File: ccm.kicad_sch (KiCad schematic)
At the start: 92 parts, among them J1 Conn_01x02_Socket, J10 Conn_01x02_Socket, J11 Conn_01x02_Socket, J12 Conn_01x02_Socket, J13 Conn_01x02_Socket, J15 Conn_01x02_Socket, J16 Conn_01x02_Socket, J17 Conn_01x02_Socket, J18 Conn_01x02_Socket, J19 Conn_01x02_Socket, J2 Conn_01x02_Socket, J20 Conn_01x02_Socket, J21 Conn_01x02_Socket, J22 Conn_01x02_Socket, J23 Conn_01x02_Socket, J24 Conn_01x02_Socket, J3 Conn_01x02_Socket, J4 Conn_01x04_Socket, J5 Conn_01x02_Socket, J6 Conn_01x02_Socket, J7 Conn_01x02_Socket, J8 Conn_01x04_Socket, J9 Conn_01x02_Socket, Q1 IRLZ34N, Q2 IRLZ34N, Q3 IRLZ34N, Q4 MMBT3904, Q5 MMBT3904, U1 Teensy4.1, U2 PAM8302AAY, U3 SN65HVD230, U4 SN65HVD230, U5 LM1117DT-5.0

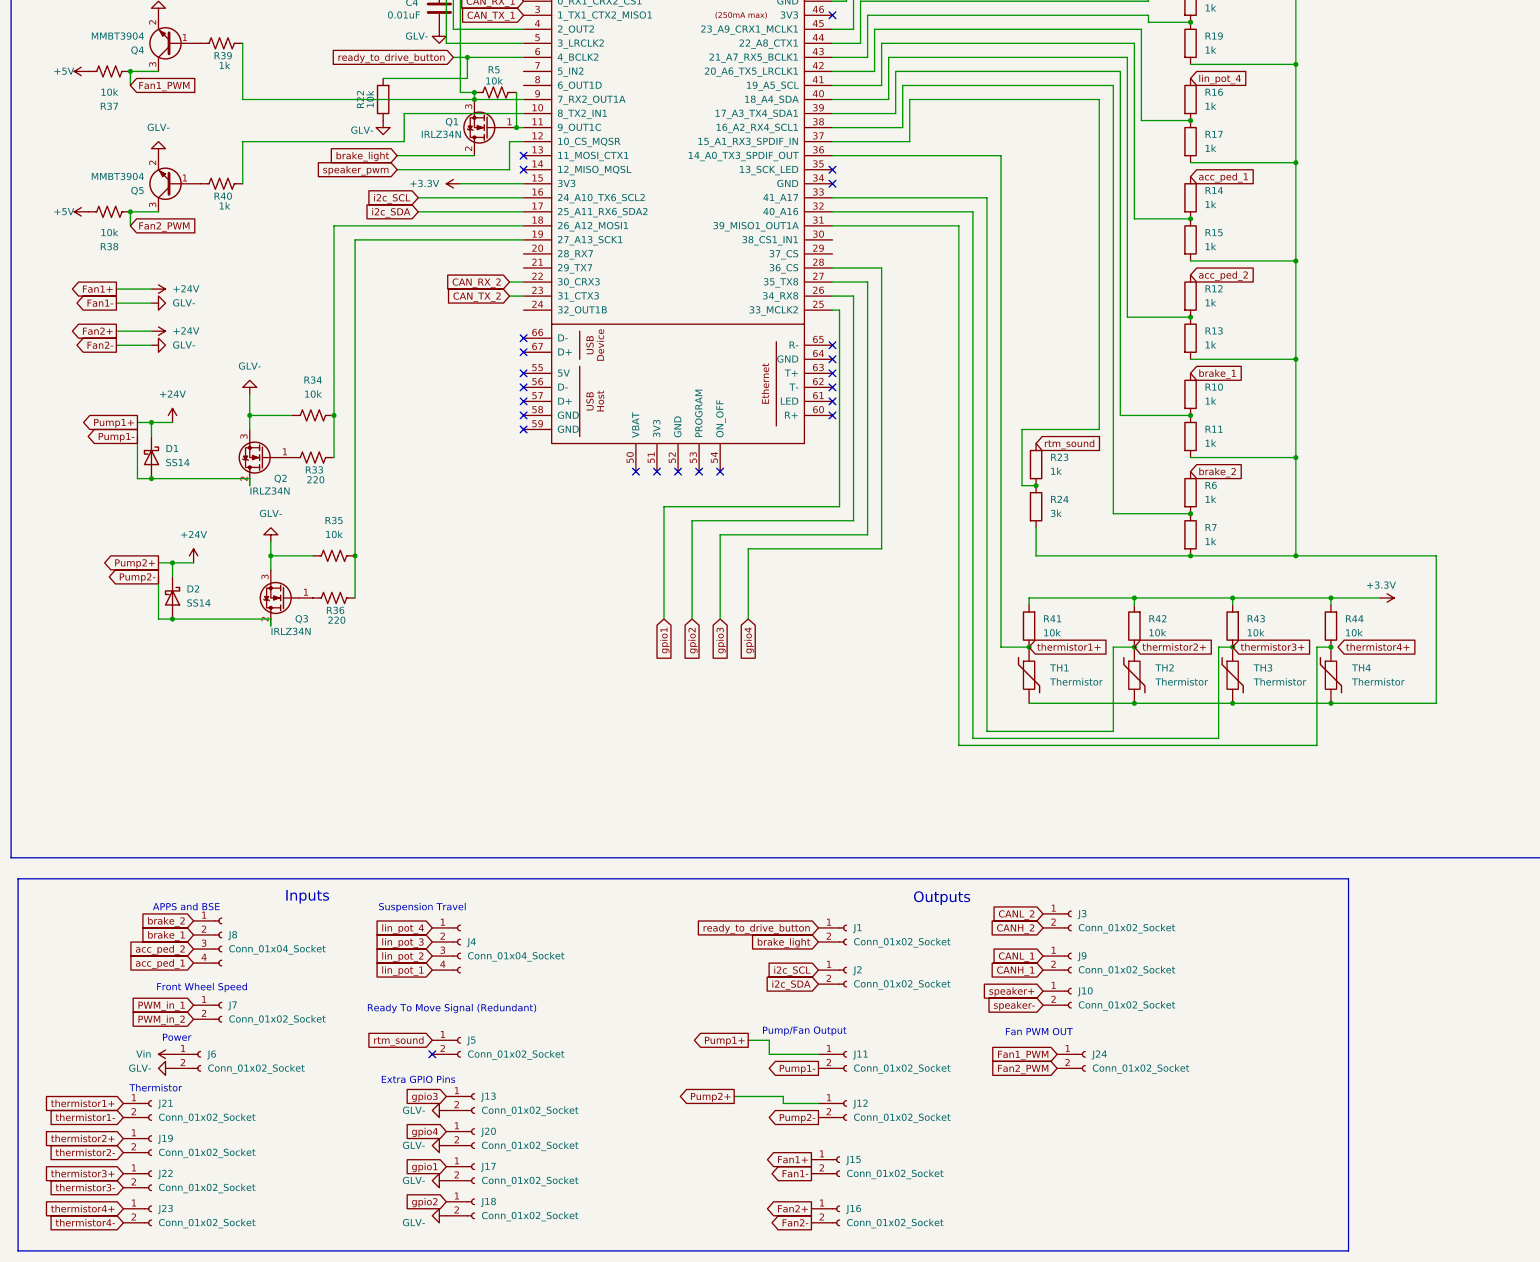
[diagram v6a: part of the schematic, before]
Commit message: leftside routing complete
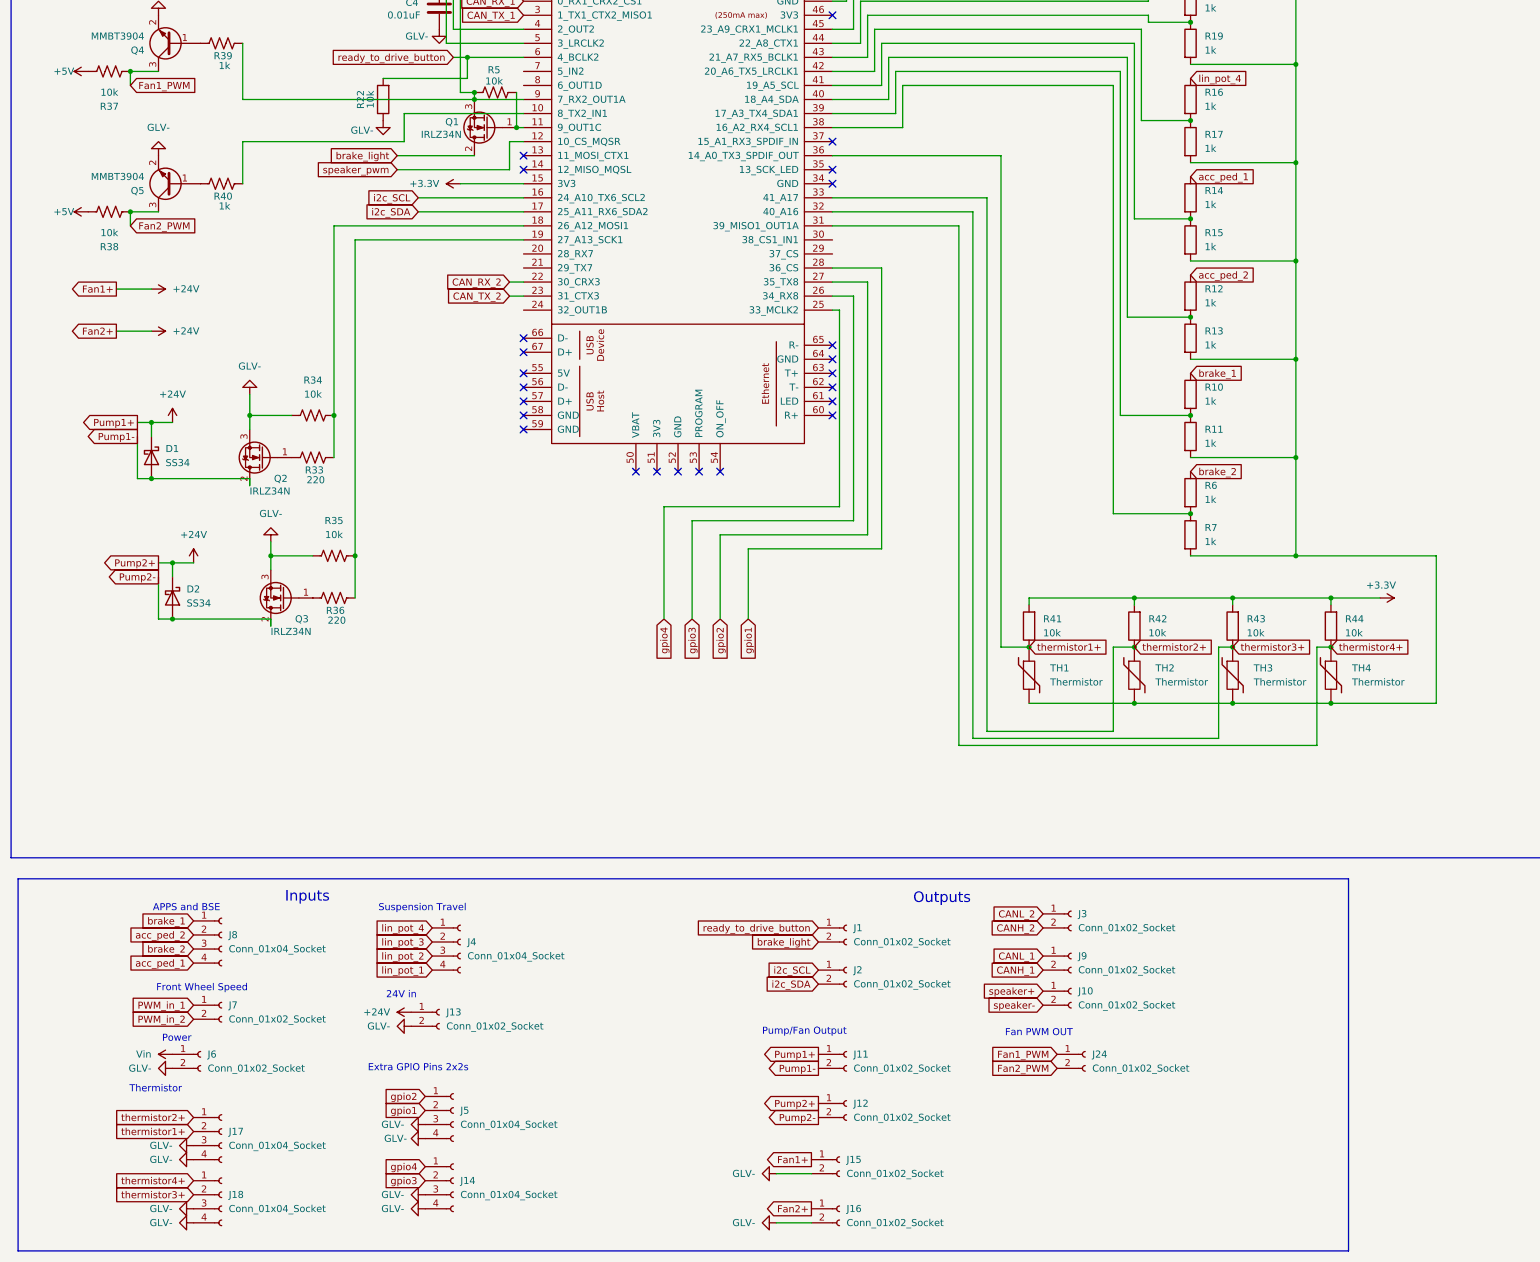
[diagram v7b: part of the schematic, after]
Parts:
- removed D1, D2: SS14, Diode_SMD:D_SMA, symbol Diode:SS14
- removed J17, J18, J19, J20, J21, J22, J23, J5: Conn_01x02_Socket, Connector_Molex:Molex_Mini-Fit_Jr_5566-02A2_2x01_P4.20mm_Vertical, symbol Connector:Conn_01x02_Socket
- removed R23: 1k, Resistor_SMD:R_0805_2012Metric, symbol Device:R
- removed R24: 3k, Resistor_SMD:R_0805_2012Metric, symbol Device:R
- added D1, D2: SS34, Diode_SMD:D_SMA, symbol Diode:SS34
- added J14, J17, J18, J5: Conn_01x04_Socket, Connector_Molex:Molex_Mini-Fit_Jr_5566-04A2_2x02_P4.20mm_Vertical, symbol Connector:Conn_01x04_Socket
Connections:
- net +24V: now also J13.1 (Pin_1), D1.1 (K), D2.1 (K)
- net GLV-: now also J14.3 (Pin_3), J14.4 (Pin_4), J17.3 (Pin_3), J17.4 (Pin_4), J18.3 (Pin_3), J18.4 (Pin_4), J5.3 (Pin_3), J5.4 (Pin_4)
- net Pump1-: now also D1.2 (A)
- net Pump2-: now also D2.2 (A)
- net acc_ped_2: now also J8.2 (Pin_2); no longer J8.3 (Pin_3)
- net brake_1: now also J8.1 (Pin_1); no longer J8.2 (Pin_2)
- net brake_2: now also J8.3 (Pin_3); no longer J8.1 (Pin_1)
- net gpio1: now also U1.28 (36_CS), J5.2 (Pin_2); no longer U1.25 (33_MCLK2)
- net gpio2: now also U1.27 (35_TX8), J5.1 (Pin_1); no longer U1.26 (34_RX8)
- net gpio3: now also U1.26 (34_RX8), J14.2 (Pin_2); no longer J13.1 (Pin_1), U1.27 (35_TX8)
- net gpio4: now also U1.25 (33_MCLK2), J14.1 (Pin_1); no longer U1.28 (36_CS)
- net thermistor1+: now also J17.2 (Pin_2)
- net thermistor2+: now also J17.1 (Pin_1)
- net thermistor3+: now also J18.2 (Pin_2)
- net thermistor4+: now also R44.1, TH4.1, U1.31 (39_MISO1_OUT1A), J18.1 (Pin_1)
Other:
- note added: "24V in"
- note added: "Extra GPIO Pins 2x2s"
- note removed: "Extra GPIO Pins"
- note removed: "Ready To Move Signal (Redundant)"

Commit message: routing v2.1 complete
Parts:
- added C10: 10nF, Capacitor_SMD:C_0805_2012Metric, symbol Device:C
- added R23: 1k, Resistor_SMD:R_0805_2012Metric, symbol Device:R_US
- R1, R10, R12, R14, R16, R18, R20, R6: value 1k -> 50k
- R11, R13, R15, R17, R19, R2, R21, R7: value 1k -> 97k
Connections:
- net Pump1- is gone; now on net GLV-: D1.2 (A), J11.2 (Pin_2), Q2.2 (D)
- net Pump2- is gone; now on net GLV-: D2.2 (A), J12.2 (Pin_2), Q3.2 (D)
- net GLV-: now also C10.1; no longer R39.2, U1.9 (7_RX2_OUT1A)
- net PWM_in_1: now also R9.1; no longer R8.1
- net PWM_in_2: now also R8.1; no longer R9.1
- net speaker_pwm: now also R23.2; no longer C7.2
- net at R40.2: now also U1.9 (7_RX2_OUT1A); no longer U1.10 (8_TX2_IN1)
- net at R35.1, R36.2: now also U1.18 (26_A12_MOSI1); no longer U1.19 (27_A13_SCK1)
- net at R33.2, R34.1: now also U1.19 (27_A13_SCK1); no longer U1.18 (26_A12_MOSI1)
- new net: C10.2, C7.2, R23.1
- new net: R39.2, U1.10 (8_TX2_IN1)
